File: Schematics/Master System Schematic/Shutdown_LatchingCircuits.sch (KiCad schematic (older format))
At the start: 6 parts, among them K2 Omron DPDT Relay, K3 Omron DPDT Relay, K4 Omron DPDT Relay, K5 Omron DPDT Relay

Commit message: Finished master and accum cleanup
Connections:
- net GLV+_Fused renamed GLV
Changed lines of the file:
@@
 $Descr A 11000 8500
 encoding utf-8
-Sheet 19 22
+Sheet 22 22
 Title "Shutdown Latching Circuits"
 Date "2020-10-12"
@@
 BMS_Latch_Reset-
 Text HLabel 3150 2250 0    50   Input ~ 0
-GLV+_Fused
+GLV
 Text HLabel 3150 2650 0    50   Input ~ 0
 Shutdown_IN

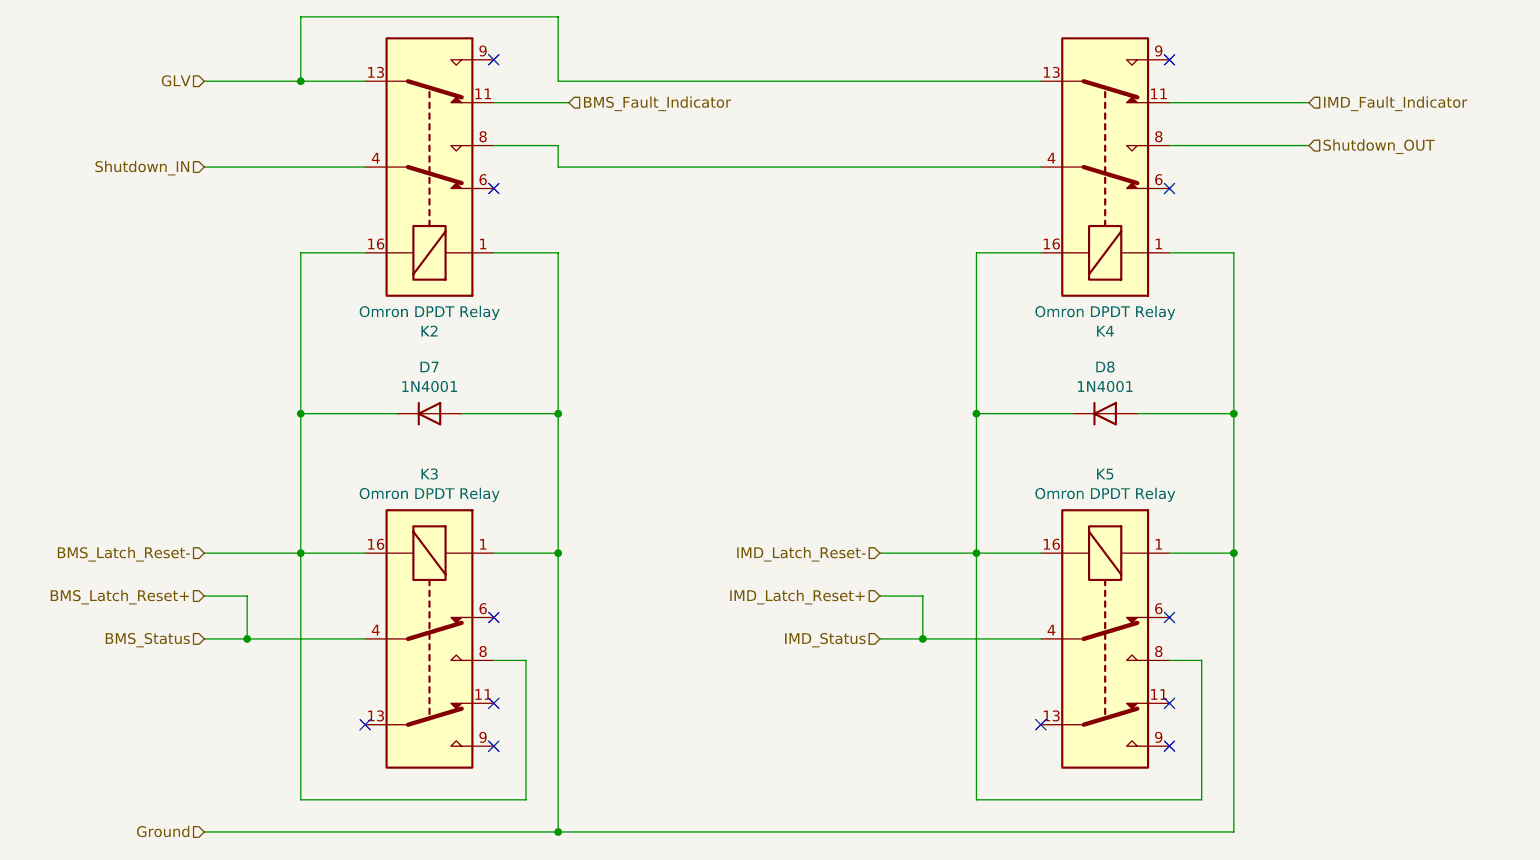
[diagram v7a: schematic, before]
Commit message: Reversed Polarity of Shutdown latch
The BMS MP_en which drives the shutdown latch is active low (ON) when there are NO faults present. When a critical DTC is present, or when a certain CANBUS message is recieved from the pedal box, the output will turn OFF (floats high), latching the relay open. If the output returns to normal (ON, active low), the relay will energize and close the shutdown loop
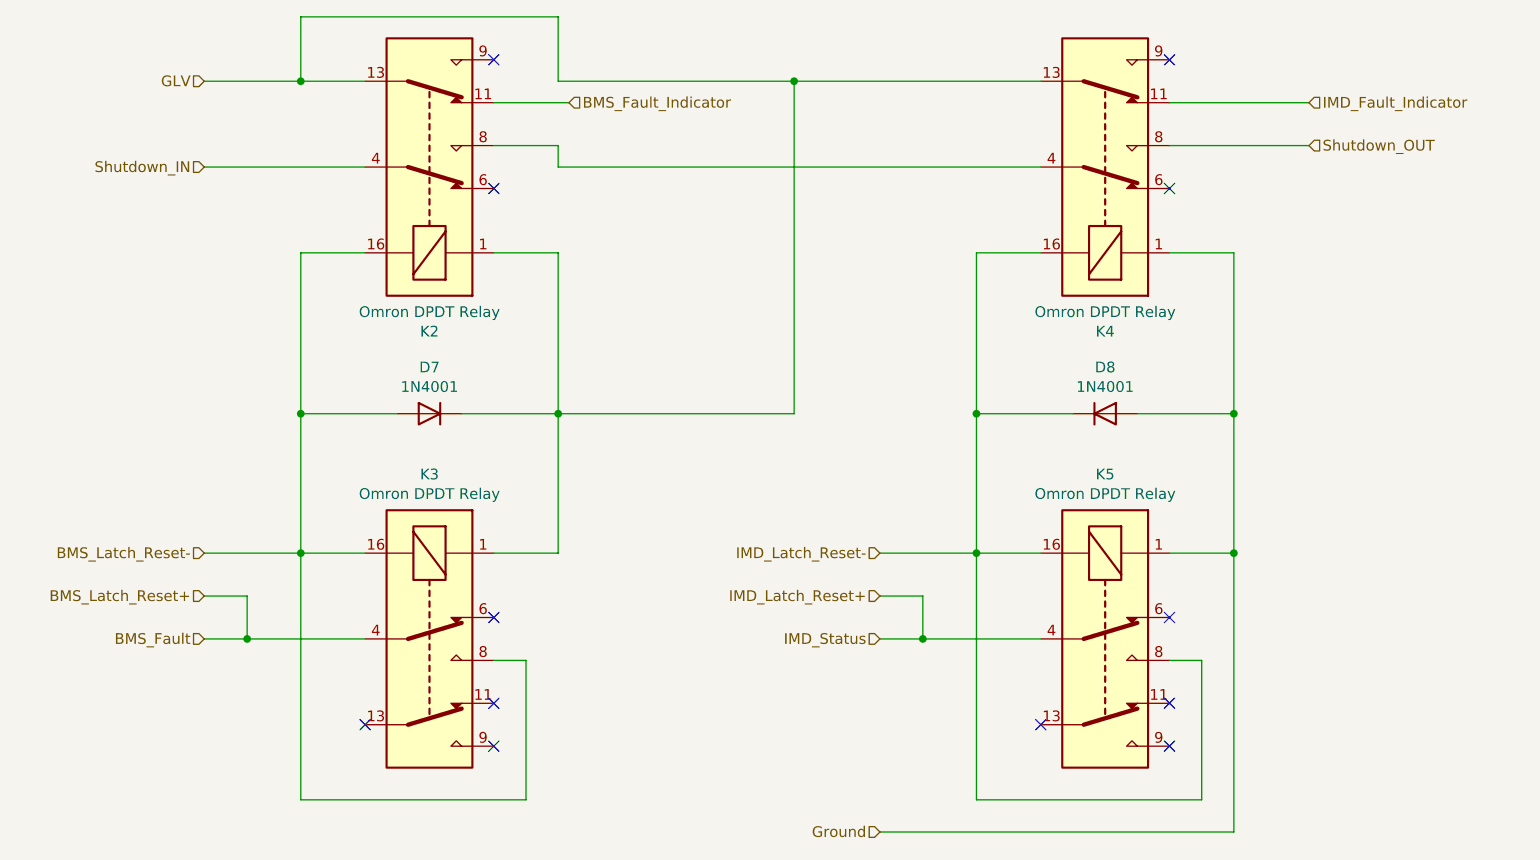
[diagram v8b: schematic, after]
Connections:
- net BMS_Latch_Reset-: now also D7.2 (A); no longer D7.1 (K)
- net GLV: now also D7.1 (K), K2.1, K3.1
- net Ground: no longer D7.2 (A), K2.1, K3.1
- net BMS_Latch_Reset+ renamed BMS_Fault
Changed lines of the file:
@@
 IMD_Latch_Reset-
 Text HLabel 3150 4850 0    50   Input ~ 0
-BMS_Status
-Text HLabel 3150 5750 0    50   Input ~ 0
+BMS_Fault
+Text HLabel 6300 5750 0    50   Input ~ 0
 Ground
 $Comp
@@
 F 3 "http://www.vishay.com/docs/88503/1n4001.pdf" H 4200 3800 50  0001 C CNN
 	1    4200 3800
-	1    0    0    -1
+	-1   0    0    -1
 $EndComp
 Wire Wire Line
@@
 	4350 3800 4800 3800
 Wire Wire Line
-	4500 3050 4800 3050
-Wire Wire Line
 	4500 4450 4800 4450
-Connection ~ 4800 4450
-Wire Wire Line
-	3150 5750 4800 5750
-Connection ~ 4800 5750
-Wire Wire Line
-	4800 5750 7950 5750
 Wire Wire Line
 	7950 4450 7950 5750
-Wire Wire Line
-	4800 4450 4800 5750
 Wire Wire Line
 	3150 2250 3600 2250
@@
 	4800 2550 4800 2650
 Wire Wire Line
-	4800 2250 7050 2250
+	4800 2250 5900 2250
 Wire Wire Line
 	4800 2650 7050 2650
@@
 	4800 3800 4800 4450
 Wire Wire Line
-	4800 3050 4800 3800
-Wire Wire Line
 	3600 3050 3600 3800
 Connection ~ 6750 3800
@@
 Wire Wire Line
 	6750 3050 6750 3800
+Wire Wire Line
+	6300 5750 7950 5750
+Wire Wire Line
+	4800 3800 5900 3800
+Wire Wire Line
+	5900 3800 5900 2250
+Connection ~ 5900 2250
+Wire Wire Line
+	5900 2250 7050 2250
+Wire Wire Line
+	4500 3050 4800 3050
+Wire Wire Line
+	4800 3050 4800 3800
 $EndSCHEMATC
